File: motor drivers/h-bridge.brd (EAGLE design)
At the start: 47.5 x 32.5 mm, 7 parts, among them IC1 L298

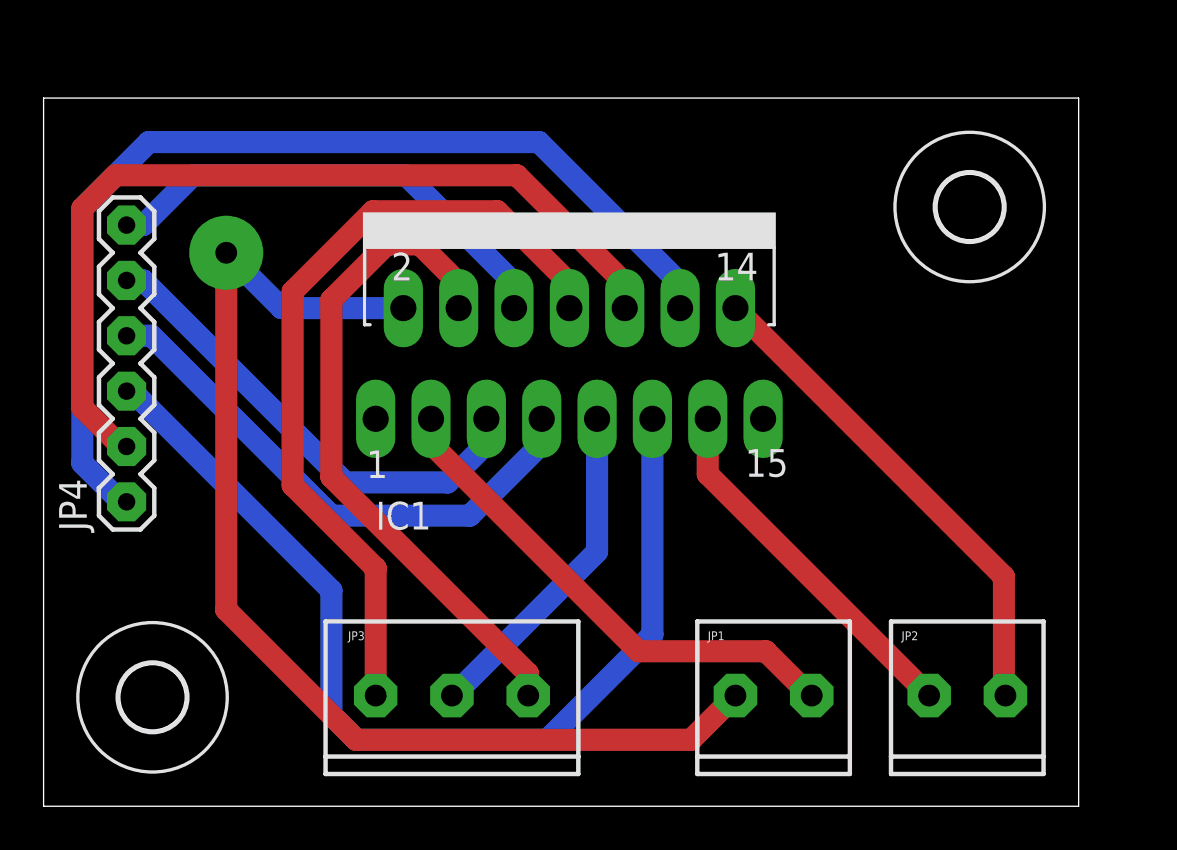
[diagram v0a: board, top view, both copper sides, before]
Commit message: fixed iv-18 boardf
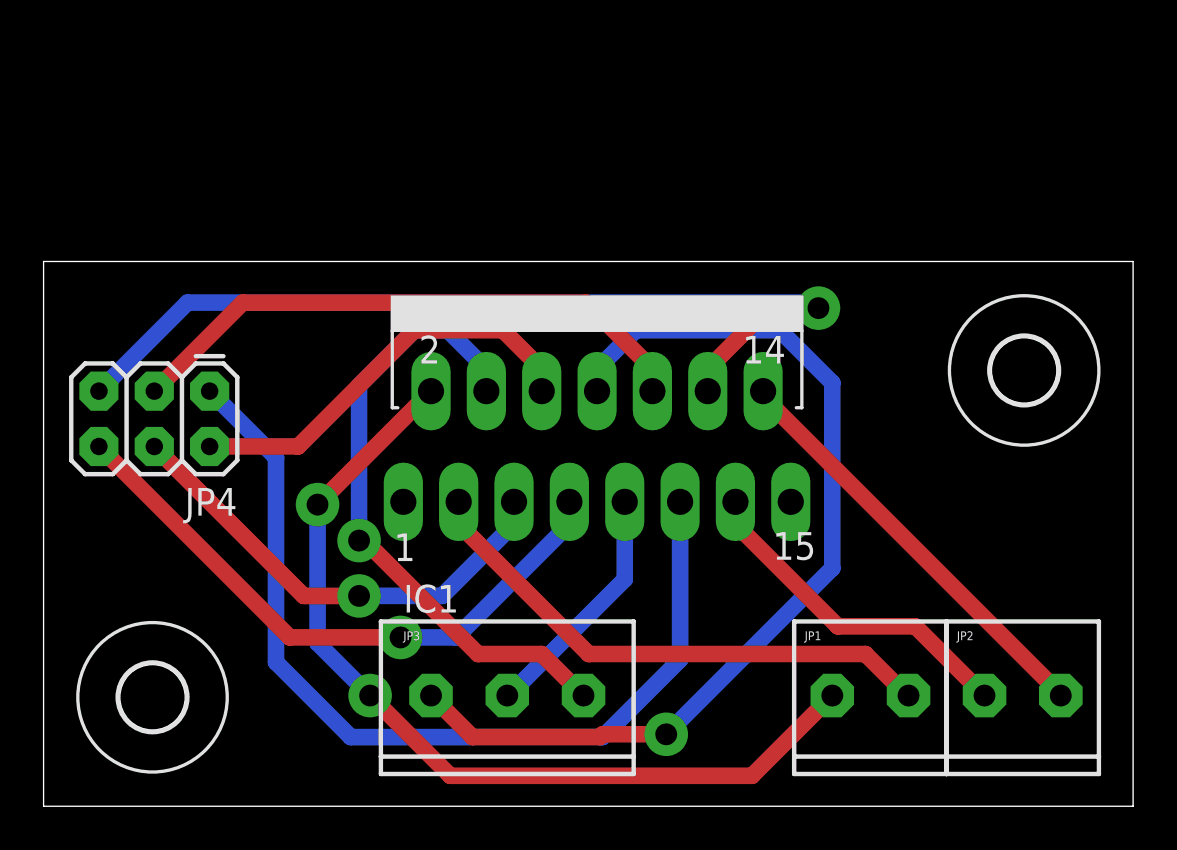
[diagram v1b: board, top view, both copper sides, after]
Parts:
- JP4: device iStivi - Header-Connector:1X06 -> iStivi - Header-Connector:2X3
- moved U$1 7.91 mm to (45.0, 20.0)
- moved JP4 6.35 mm to (7.62, 19.1), turned to 180 degrees
- moved JP1 4.45 mm to (36.2, 5.08)
- moved IC1 4.02 mm to (25.4, 21.6)
- moved JP3 2.54 mm to (17.8, 5.08)
- moved JP2 2.54 mm to (43.2, 5.08)
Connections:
- net N$10: now also JP4.6; no longer JP4.4
- net N$11: now also JP4.1; no longer JP4.3
- net N$12: now also JP4.3; no longer JP4.2
- net N$13: now also JP4.5; no longer JP4.1
- net N$8: now also JP4.2; no longer JP4.6
- net N$9: now also JP4.4; no longer JP4.5
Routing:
- net N$12: track 40.6 -> 26.8 mm
- net N$1: track 52.2 -> 41.4 mm, vias 1 -> 2
- net N$5: track 36.9 -> 44.5 mm, vias 0 -> 1
- net N$13: track 47.0 -> 42.1 mm, vias 0 -> 1
- net N$7: track 15.5 -> 11.2 mm
- net N$11: track 46.0 -> 42.4 mm
- net N$10: track 25.0 -> 28.4 mm, vias 0 -> 1
- net N$4: track 23.0 -> 19.7 mm
- net N$8: track 21.9 -> 19.2 mm
- net N$6: track 30.7 -> 29.0 mm, vias 0 -> 1
- net N$2: track 23.4 -> 24.9 mm
- net N$3: track 16.9 -> 15.7 mm
- net N$9: track 22.2 -> 21.7 mm, vias 0 -> 1
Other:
- board size 47.5 x 32.5 mm -> 50 x 25 mm

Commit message: finished routing h-bridge board
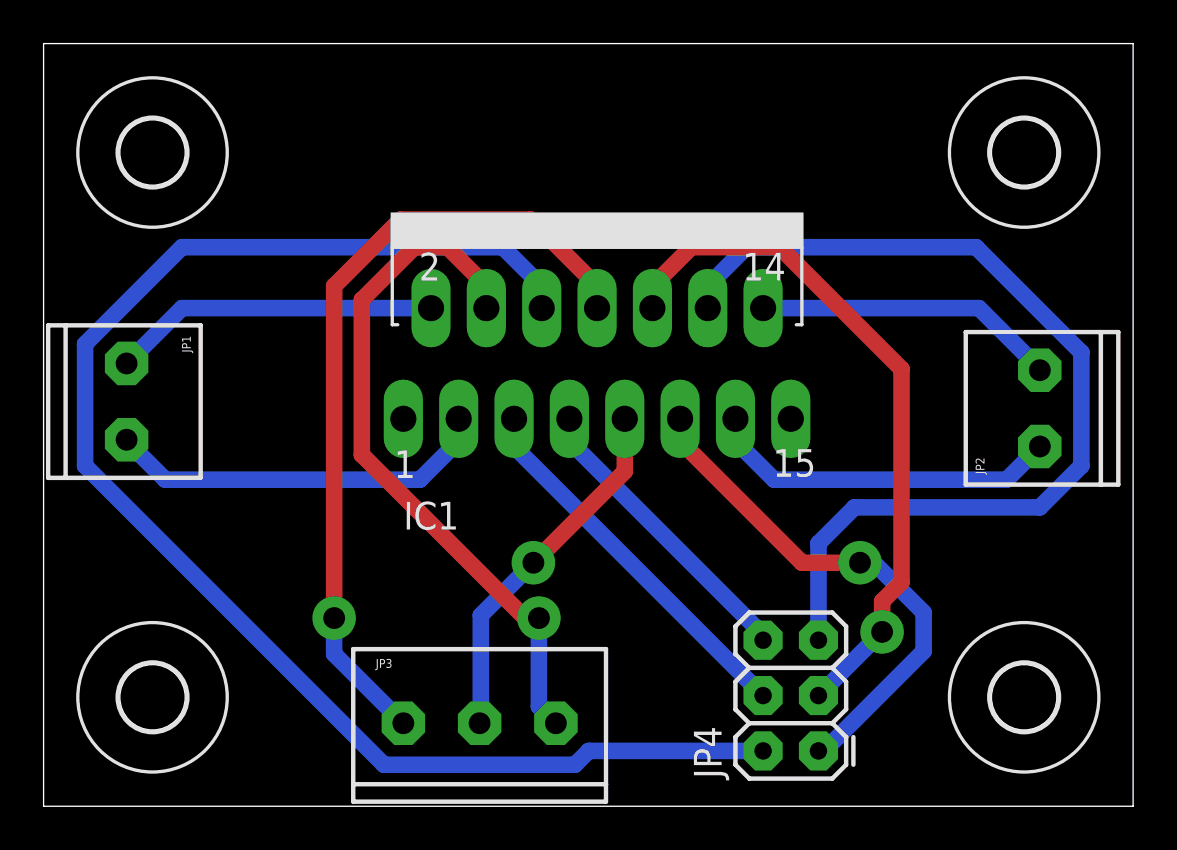
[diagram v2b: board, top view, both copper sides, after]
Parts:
- added U$3, U$4: (no value), iStivi - Board-Holes:3,0
- moved JP1 35.8 mm to (3.81, 20.3), turned to 270 degrees
- moved JP4 32.5 mm to (35.6, 2.54), turned to 90 degrees
- moved JP2 11.7 mm to (45.7, 16.5), turned to 90 degrees
- moved U$1 10.0 mm to (45.0, 30.0)
- moved IC1 3.81 mm to (25.4, 25.4)
- moved JP3 1.80 mm to (16.5, 3.81)
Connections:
- net N$1 renamed A_OUT1
- net N$10 renamed A_2
- net N$11 renamed B_EN
- net N$12 renamed B_1
- net N$13 renamed B_2
- net N$2 renamed A_OUT2
- net N$3 renamed B_OUT1
- net N$4 renamed B_OUT2
- net N$5 renamed GND
- net N$6 renamed VS
- net N$7 renamed VCC
- net N$8 renamed A_EN
- net N$9 renamed A_1
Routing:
- net A_EN: track 19.2 -> 67.2 mm
- net A_OUT1: track 41.4 -> 15.0 mm, vias 2 -> 0
- net B_EN: track 42.4 -> 24.0 mm, vias 0 -> 1
- net A_2: track 28.4 -> 13.8 mm, vias 1 -> 0
- net GND: track 44.5 -> 37.0 mm
- net A_OUT2: track 24.9 -> 17.8 mm
- net B_OUT2: track 19.7 -> 13.9 mm
- net VCC: track 11.2 -> 16.8 mm, vias 0 -> 1
- net B_1: track 26.8 -> 32.1 mm, vias 0 -> 1
- net A_1: track 21.7 -> 17.4 mm, vias 1 -> 0
- net VS: track 29.0 -> 32.0 mm
- net B_2: track 42.1 -> 44.1 mm, vias 1 -> 0
- net B_OUT1: track 15.7 -> 16.4 mm
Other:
- board size 50 x 25 mm -> 50 x 35 mm
